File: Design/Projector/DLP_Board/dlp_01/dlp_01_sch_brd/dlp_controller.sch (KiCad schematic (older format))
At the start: 0 parts

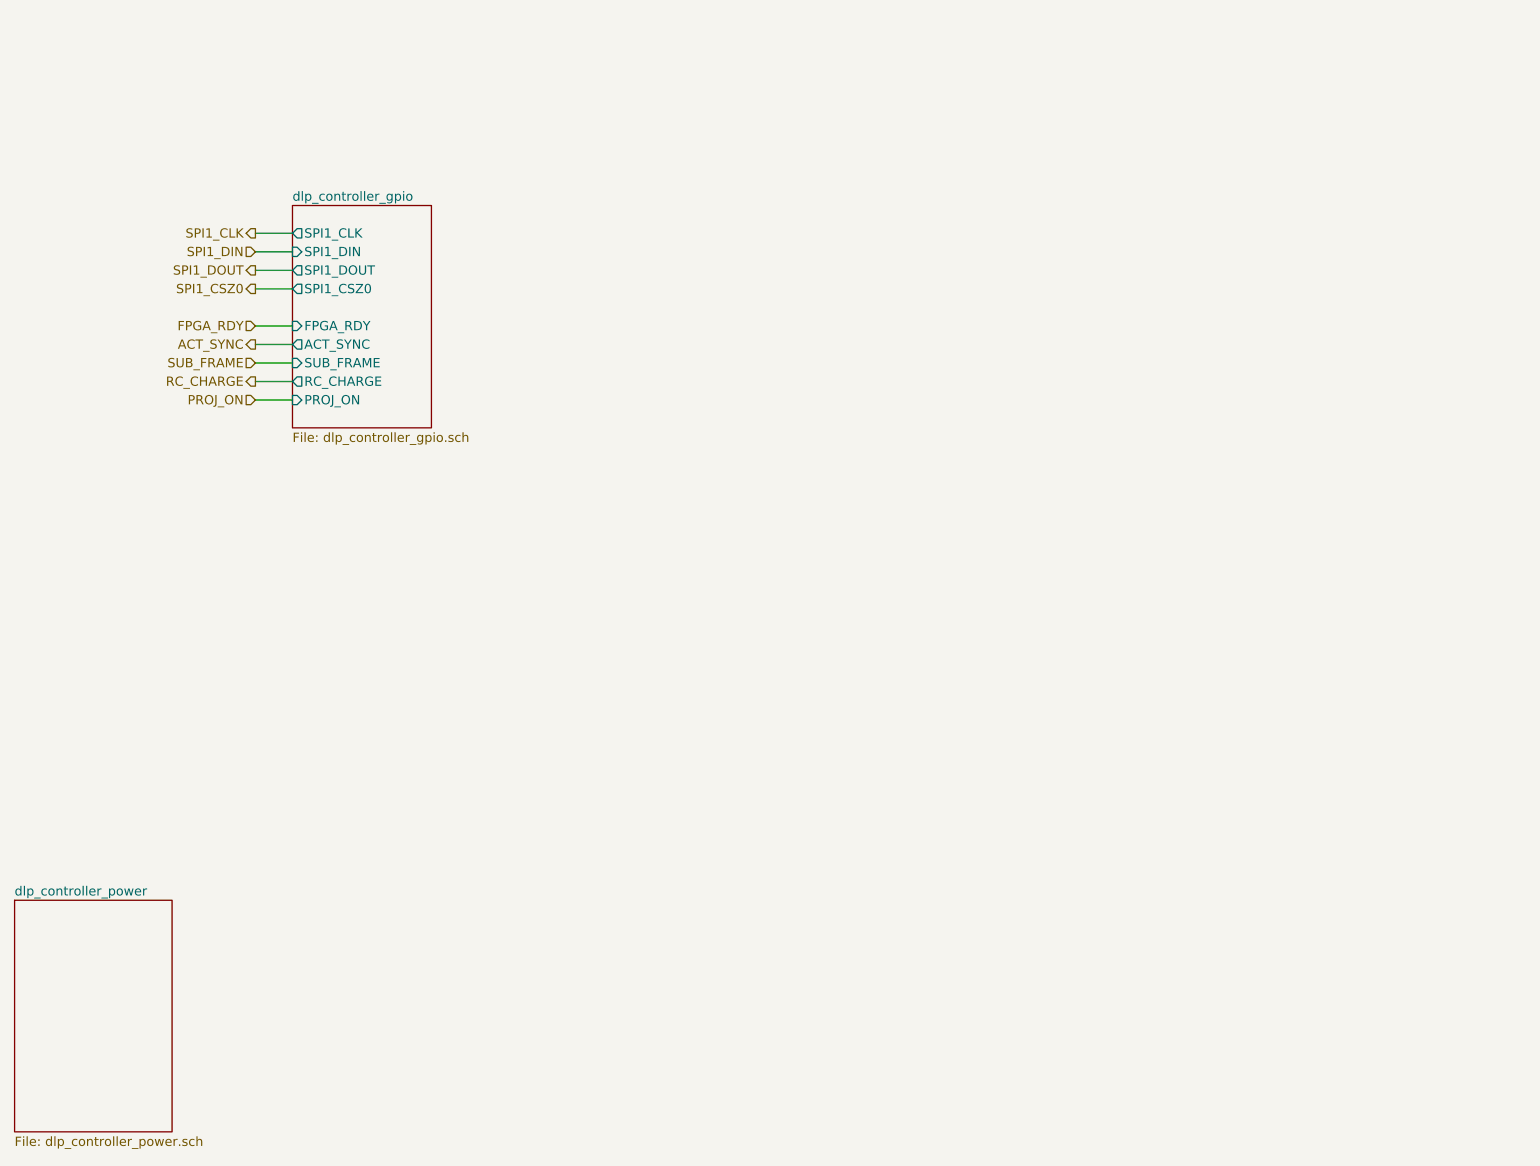
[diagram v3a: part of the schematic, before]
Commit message: Initial placement of power converters, BGA fanout and Z-turn board outline imported
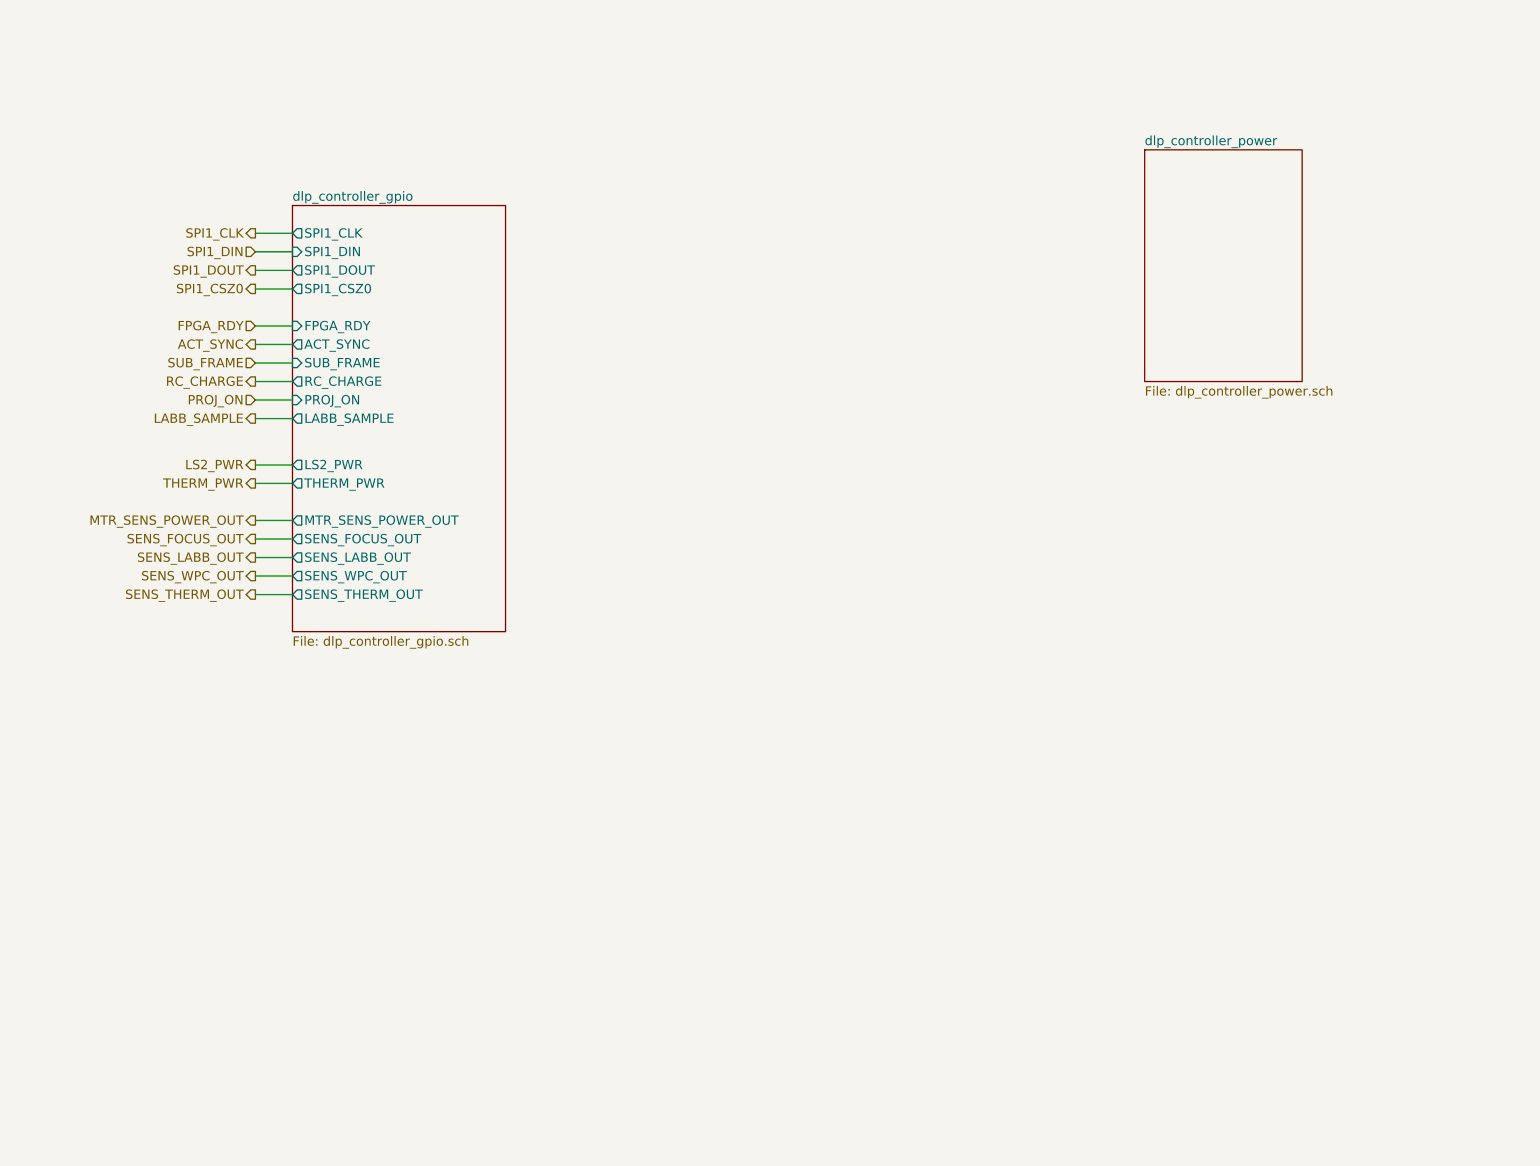
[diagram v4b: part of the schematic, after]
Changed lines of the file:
@@
 $Descr A3 16535 11693
 encoding utf-8
-Sheet 2 10
+Sheet 2 11
 Title ""
 Date ""
@@
 $EndDescr
 $Sheet
-S 1400 9300 850  1250
+S 7500 5250 850  1250
 U 5CFF2D84
 F0 "dlp_controller_power" 50
@@
 $EndSheet
 $Sheet
-S 2900 5550 750  1200
+S 2900 5550 1150 2300
 U 5D57FAF8
 F0 "dlp_controller_gpio" 50
@@
 F9 "SPI1_CLK" O L 2900 5700 50
 F10 "SPI1_DIN" I L 2900 5800 50
+F11 "LABB_SAMPLE" O L 2900 6700 50
+F13 "MTR_SENS_POWER_OUT" O L 2900 7250 50
+F14 "SENS_FOCUS_OUT" O L 2900 7350 50
+F15 "LS2_PWR" O L 2900 6950 50
+F16 "SENS_LABB_OUT" O L 2900 7450 50
+F17 "SENS_WPC_OUT" O L 2900 7550 50
+F18 "SENS_THERM_OUT" O L 2900 7650 50
+F19 "THERM_PWR" O L 2900 7050 50
 $EndSheet
 $Sheet
@@
 NoConn ~ 2350 2450
 NoConn ~ 2350 2550
+Text HLabel 2700 6700 0    50   Output ~ 0
+LABB_SAMPLE
+Wire Wire Line
+	2700 6700 2900 6700
+Text HLabel 2700 6950 0    50   Output ~ 0
+LS2_PWR
+Text HLabel 2700 7050 0    50   Output ~ 0
+THERM_PWR
+Text HLabel 2700 7250 0    50   Output ~ 0
+MTR_SENS_POWER_OUT
+Text HLabel 2700 7350 0    50   Output ~ 0
+SENS_FOCUS_OUT
+Text HLabel 2700 7450 0    50   Output ~ 0
+SENS_LABB_OUT
+Text HLabel 2700 7550 0    50   Output ~ 0
+SENS_WPC_OUT
+Text HLabel 2700 7650 0    50   Output ~ 0
+SENS_THERM_OUT
+Wire Wire Line
+	2700 6950 2900 6950
+Wire Wire Line
+	2900 7050 2700 7050
+Wire Wire Line
+	2700 7250 2900 7250
+Wire Wire Line
+	2900 7350 2700 7350
+Wire Wire Line
+	2700 7450 2900 7450
+Wire Wire Line
+	2700 7550 2900 7550
+Wire Wire Line
+	2900 7650 2700 7650
 $EndSCHEMATC
